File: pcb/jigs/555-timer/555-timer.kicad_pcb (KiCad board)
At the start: 2 copper layers, 16.5 x 15.5 mm, 17 parts, among them J1 Pin headers, J2 Pin headers, U1 NE555

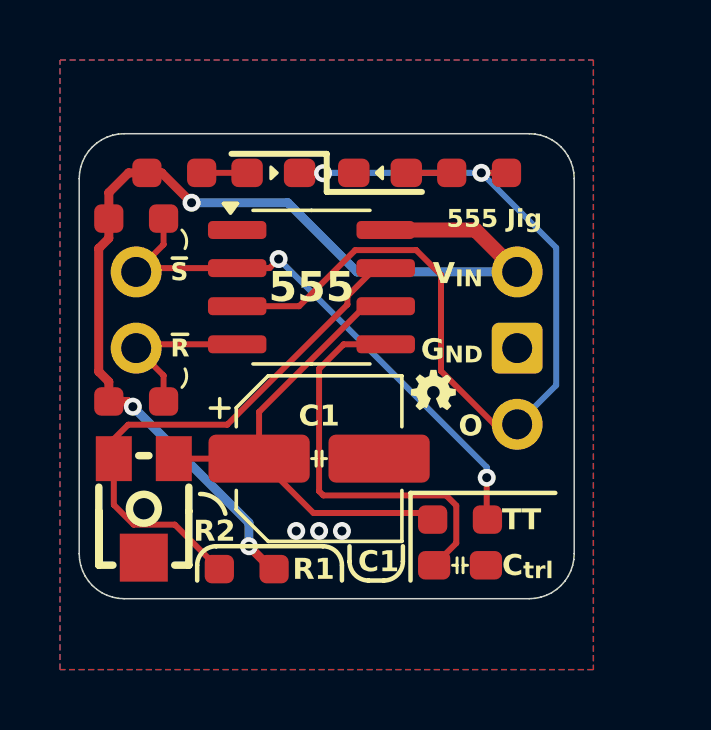
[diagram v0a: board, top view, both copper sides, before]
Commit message: Fix indicator LED order on 555-timer jig
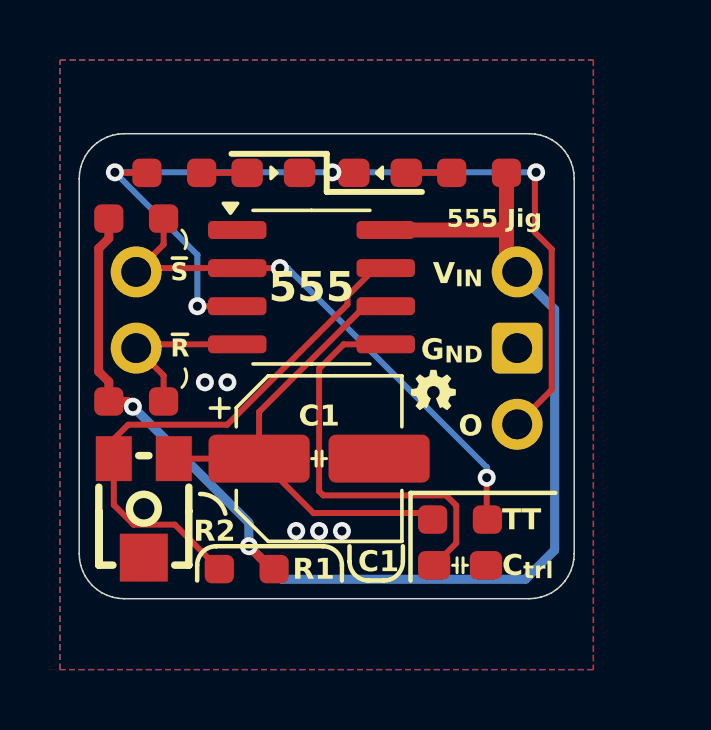
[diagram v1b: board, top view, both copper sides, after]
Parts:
- moved R5 10.2 mm to (135.9, 80.5), turned to 180 degrees
- moved R6 10.2 mm to (125.7, 80.5), turned to 0 degrees
- moved LED1 3.56 mm to (132.6, 80.5), turned to 0 degrees
- moved LED2 3.56 mm to (129.0, 80.5), turned to 180 degrees
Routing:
- net +5V: track 35.7 -> 43.0 mm, vias 3 -> 2
- net Output: track 31.2 -> 31.9 mm, vias 2 -> 4
- net GND: vias 3 -> 5

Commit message: Fix potentiometer pinout on 555-timer jig
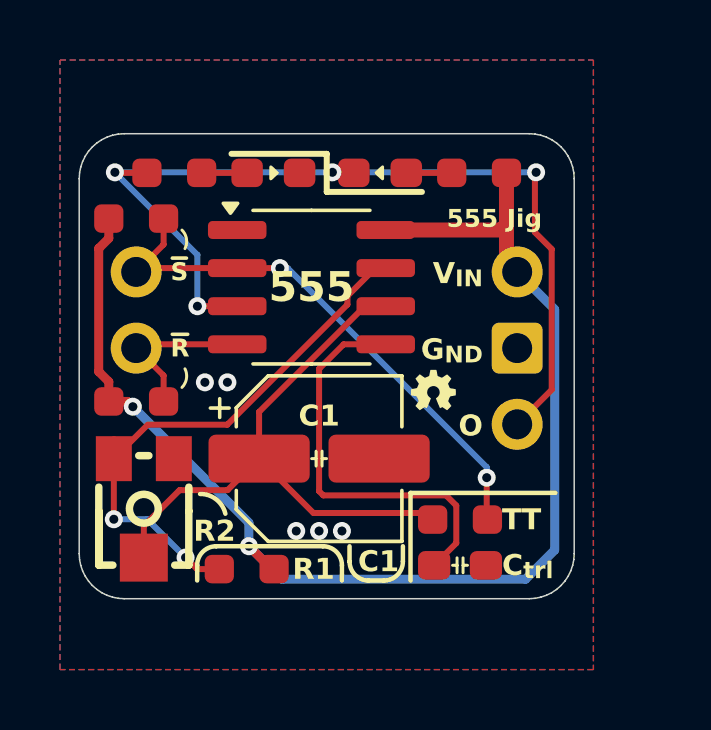
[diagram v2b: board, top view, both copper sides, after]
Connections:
- RV1 pad 1: Net-(U1-Threshold) -> unconnected-(RV1-Pad1)
- RV1 pad 2: unconnected-(RV1-Pad2) -> Net-(U1-Threshold)
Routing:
- net Net-(U1-Threshold): track 16.7 -> 19.7 mm
- net Net-(U1-Discharge): track 18.2 -> 18.7 mm, vias 0 -> 2
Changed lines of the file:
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@@
 	(net 9 "Net-(LED1-A)")
 	(net 10 "Net-(LED2-A)")
-	(net 11 "unconnected-(RV1-Pad2)")
+	(net 11 "unconnected-(RV1-Pad1)")
 	(footprint "custom:C_0603_1608Metric_Pad1.08x0.95mm_HandSolder"
 		(layer "F.Cu")
@@
 			(size 1.2 1.5)
 			(layers "F.Cu" "F.Paste" "F.Mask")
-			(net 3 "Net-(U1-Threshold)")
+			(net 11 "unconnected-(RV1-Pad1)")
 			(pinfunction "1")
-			(pintype "passive")
+			(pintype "passive+no_connect")
 		)
 		(pad "2" smd rect
@@
 			(size 1.6 1.6)
 			(layers "F.Cu" "F.Paste" "F.Mask")
-			(net 11 "unconnected-(RV1-Pad2)")
+			(net 3 "Net-(U1-Threshold)")
 			(pinfunction "2")
-			(pintype "passive+no_connect")
+			(pintype "passive")
 		)
 		(pad "3" smd rect
@@
 	)
 	(segment
-		(start 128.555 90.044)
-		(end 128.556 90.043)
-		(width 0.2)
-		(layer "F.Cu")
-		(net 3)
-	)
-	(segment
 		(start 128.556 90.043)
 		(end 128.556 88.487)
@@
 	)
 	(segment
-		(start 125.714 90.044)
-		(end 128.555 90.044)
+		(start 132.08 84.963)
+		(end 132.777 84.963)
 		(width 0.2)
 		(layer "F.Cu")
@@
 	)
 	(segment
-		(start 132.08 84.963)
-		(end 132.777 84.963)
+		(start 127.505 91.094)
+		(end 125.906 91.094)
 		(width 0.2)
 		(layer "F.Cu")
@@
 	)
 	(segment
-		(start 130.369 91.856)
-		(end 134.1235 91.856)
+		(start 128.556 90.043)
+		(end 127.505 91.094)
 		(width 0.2)
 		(layer "F.Cu")
@@
 	)
 	(segment
-		(start 123.714 91.583)
-		(end 124.375 92.244)
+		(start 124.714 92.286)
+		(end 124.714 93.344)
 		(width 0.2)
 		(layer "F.Cu")
-		(net 4)
+		(net 3)
 	)
 	(segment
-		(start 124.375 92.244)
-		(end 125.7485 92.244)
+		(start 125.906 91.094)
+		(end 124.714 92.286)
 		(width 0.2)
 		(layer "F.Cu")
-		(net 4)
+		(net 3)
 	)
 	(segment
-		(start 123.714 89.392)
-		(end 124.193 88.913)
+		(start 130.369 91.856)
+		(end 134.1235 91.856)
+		(width 0.2)
+		(layer "F.Cu")
+		(net 3)
+	)
+	(segment
+		(start 127.495 88.913)
+		(end 124.845 88.913)
 		(width 0.2)
 		(layer "F.Cu")
@@
 	)
 	(segment
+		(start 124.845 88.913)
+		(end 123.714 90.044)
+		(width 0.2)
+		(layer "F.Cu")
+		(net 4)
+	)
+	(segment
 		(start 127.495 88.913)
 		(end 131.502 84.906)
@@
 	)
 	(segment
+		(start 123.714 92.063763)
+		(end 123.714 90.044)
+		(width 0.2)
+		(layer "F.Cu")
+		(net 4)
+	)
+	(segment
 		(start 131.502 84.906)
 		(end 131.502 84.622448)
@@
 	)
 	(segment
-		(start 125.7485 92.244)
-		(end 127.2305 93.726)
+		(start 127.2305 93.726)
+		(end 126.490002 93.726)
 		(width 0.2)
 		(layer "F.Cu")
@@
 	)
 	(segment
-		(start 124.193 88.913)
-		(end 127.495 88.913)
+		(start 126.490002 93.726)
+		(end 126.105766 93.341764)
 		(width 0.2)
 		(layer "F.Cu")
 		(net 4)
 	)
+	(via
+		(at 126.105766 93.341764)
+		(size 0.6)
+		(drill 0.3)
+		(layers "F.Cu" "B.Cu")
+		(net 4)
+	)
+	(via
+		(at 123.714 92.063763)
+		(size 0.6)
+		(drill 0.3)
+		(layers "F.Cu" "B.Cu")
+		(net 4)
+	)
 	(segment
-		(start 123.714 90.044)
-		(end 123.714 91.583)
+		(start 124.827765 92.063763)
+		(end 126.105766 93.341764)
 		(width 0.2)
-		(layer "F.Cu")
+		(layer "B.Cu")
+		(net 4)
+	)
+	(segment
+		(start 123.714 92.063763)
+		(end 124.827765 92.063763)
+		(width 0.2)
+		(layer "B.Cu")
 		(net 4)
 	)

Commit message: Update 555-timer jig silkscreen info
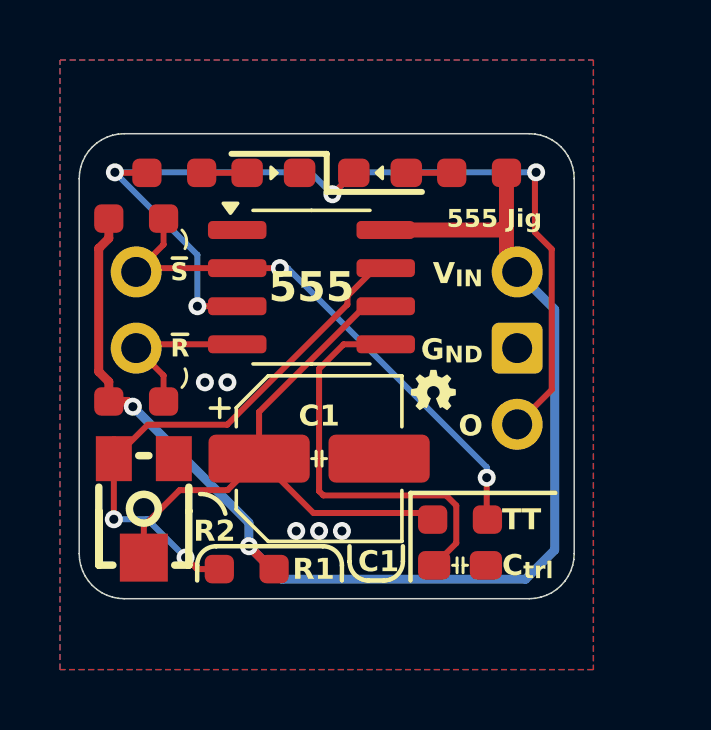
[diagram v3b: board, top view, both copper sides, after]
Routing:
- net Output: track 31.9 -> 32.8 mm
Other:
- board text added: "pcb.smkent.net"
- board text added: "rev 2"
- board text removed: "github.com/smkent/pcb"

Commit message: Change 555-timer jig front title string and font
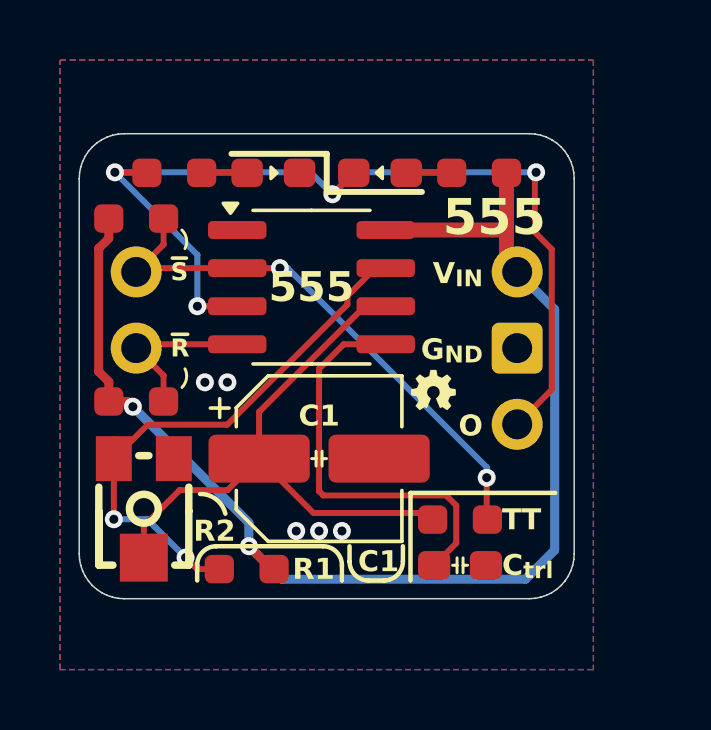
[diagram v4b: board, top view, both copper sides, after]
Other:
- board text removed: "555 Jig"
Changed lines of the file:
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@@
 		)
 	)
-	(gr_text "555 Jig"
-		(at 136.398 82.042 0)
+	(gr_text "555"
+		(at 136.398 82 0)
 		(layer "F.SilkS")
 		(effects
 			(font
-				(size 0.6 0.6)
+				(face "Bitter Black")
+				(size 1.2 1.2)
 				(thickness 0.2)
 				(bold yes)
 			)
 		)
+		(render_cache "555" 0
+			(polygon
+				(pts
+					(xy 135.431384 82.519981) (xy 135.367919 82.517641) (xy 135.303552 82.510622) (xy 135.238283 82.498923)
+					(xy 135.172113 82.482544) (xy 135.105041 82.461485) (xy 135.037068 82.435746) (xy 135.009626 82.42414)
+					(xy 135.098726 82.188788) (xy 135.157307 82.21143) (xy 135.215889 82.230298) (xy 135.242927 82.237734)
+					(xy 135.303971 82.250357) (xy 135.364271 82.256037) (xy 135.375697 82.256199) (xy 135.435316 82.249827)
+					(xy 135.458935 82.242717) (xy 135.508502 82.209324) (xy 135.515209 82.200805) (xy 135.534464 82.144655)
+					(xy 135.535432 82.124894) (xy 135.5251 82.066349) (xy 135.494106 82.028467) (xy 135.437558 82.004098)
+					(xy 135.379214 81.994762) (xy 135.320481 81.991189) (xy 135.260777 81.989363) (xy 135.207756 81.9889)
+					(xy 135.080261 81.9889) (xy 135.103708 81.305117) (xy 135.841126 81.305117) (xy 135.836144 81.565676)
+					(xy 135.345509 81.565676) (xy 135.441349 81.508523) (xy 135.424643 81.814217) (xy 135.337302 81.743582)
+					(xy 135.439591 81.743582) (xy 135.501374 81.745179) (xy 135.567098 81.75108) (xy 135.625979 81.761328)
+					(xy 135.68489 81.778364) (xy 135.710994 81.789011) (xy 135.762691 81.817347) (xy 135.809529 81.855358)
+					(xy 135.848157 81.905103) (xy 135.853729 81.915041) (xy 135.878092 81.973639) (xy 135.891464 82.032441)
+					(xy 135.896479 82.096509) (xy 135.89652 82.103205) (xy 135.893589 82.163254) (xy 135.883061 82.226008)
+					(xy 135.864875 82.282496) (xy 135.835264 82.338558) (xy 135.797284 82.386711) (xy 135.752255 82.427306)
+					(xy 135.700179 82.460343) (xy 135.668202 82.475431) (xy 135.606693 82.496967) (xy 135.54867 82.510193)
+					(xy 135.487496 82.51785)
+				)
+			)
+			(polygon
+				(pts
+					(xy 136.370449 82.519981) (xy 136.306984 82.517641) (xy 136.242617 82.510622) (xy 136.177348 82.498923)
+					(xy 136.111178 82.482544) (xy 136.044106 82.461485) (xy 135.976133 82.435746) (xy 135.948691 82.42414)
+					(xy 136.03779 82.188788) (xy 136.096372 82.21143) (xy 136.154954 82.230298) (xy 136.181991 82.237734)
+					(xy 136.243036 82.250357) (xy 136.303336 82.256037) (xy 136.314762 82.256199) (xy 136.374381 82.249827)
+					(xy 136.398 82.242717) (xy 136.447567 82.209324) (xy 136.454273 82.200805) (xy 136.473529 82.144655)
+					(xy 136.474497 82.124894) (xy 136.464165 82.066349) (xy 136.433171 82.028467) (xy 136.376622 82.004098)
+					(xy 136.318279 81.994762) (xy 136.259546 81.991189) (xy 136.199842 81.989363) (xy 136.146821 81.9889)
+					(xy 136.019326 81.9889) (xy 136.042773 81.305117) (xy 136.780191 81.305117) (xy 136.775209 81.565676)
+					(xy 136.284573 81.565676) (xy 136.380414 81.508523) (xy 136.363708 81.814217) (xy 136.276367 81.743582)
+					(xy 136.378656 81.743582) (xy 136.440439 81.745179) (xy 136.506163 81.75108) (xy 136.565044 81.761328)
+					(xy 136.623955 81.778364) (xy 136.650058 81.789011) (xy 136.701756 81.817347) (xy 136.748594 81.855358)
+					(xy 136.787222 81.905103) (xy 136.792794 81.915041) (xy 136.817157 81.973639) (xy 136.830529 82.032441)
+					(xy 136.835544 82.096509) (xy 136.835585 82.103205) (xy 136.832654 82.163254) (xy 136.822126 82.226008)
+					(xy 136.80394 82.282496) (xy 136.774329 82.338558) (xy 136.736349 82.386711) (xy 136.69132 82.427306)
+					(xy 136.639244 82.460343) (xy 136.607267 82.475431) (xy 136.545757 82.496967) (xy 136.487734 82.510193)
+					(xy 136.426561 82.51785)
+				)
+			)
+			(polygon
+				(pts
+					(xy 137.309514 82.519981) (xy 137.246049 82.517641) (xy 137.181682 82.510622) (xy 137.116413 82.498923)
+					(xy 137.050243 82.482544) (xy 136.983171 82.461485) (xy 136.915197 82.435746) (xy 136.887756 82.42414)
+					(xy 136.976855 82.188788) (xy 137.035437 82.21143) (xy 137.094019 82.230298) (xy 137.121056 82.237734)
+					(xy 137.182101 82.250357) (xy 137.242401 82.256037) (xy 137.253827 82.256199) (xy 137.313446 82.249827)
+					(xy 137.337065 82.242717) (xy 137.386632 82.209324) (xy 137.393338 82.200805) (xy 137.412594 82.144655)
+					(xy 137.413562 82.124894) (xy 137.40323 82.066349) (xy 137.372236 82.028467) (xy 137.315687 82.004098)
+					(xy 137.257344 81.994762) (xy 137.198611 81.991189) (xy 137.138907 81.989363) (xy 137.085885 81.9889)
+					(xy 136.958391 81.9889) (xy 136.981838 81.305117) (xy 137.719256 81.305117) (xy 137.714273 81.565676)
+					(xy 137.223638 81.565676) (xy 137.319479 81.508523) (xy 137.302773 81.814217) (xy 137.215432 81.743582)
+					(xy 137.317721 81.743582) (xy 137.379503 81.745179) (xy 137.445228 81.75108) (xy 137.504109 81.761328)
+					(xy 137.56302 81.778364) (xy 137.589123 81.789011) (xy 137.640821 81.817347) (xy 137.687658 81.855358)
+					(xy 137.726287 81.905103) (xy 137.731859 81.915041) (xy 137.756222 81.973639) (xy 137.769594 82.032441)
+					(xy 137.774608 82.096509) (xy 137.77465 82.103205) (xy 137.771719 82.163254) (xy 137.761191 82.226008)
+					(xy 137.743005 82.282496) (xy 137.713394 82.338558) (xy 137.675414 82.386711) (xy 137.630385 82.427306)
+					(xy 137.578309 82.460343) (xy 137.546332 82.475431) (xy 137.484822 82.496967) (xy 137.426799 82.510193)
+					(xy 137.365626 82.51785)
+				)
+			)
+		)

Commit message: Update PCB projects for footprint updates
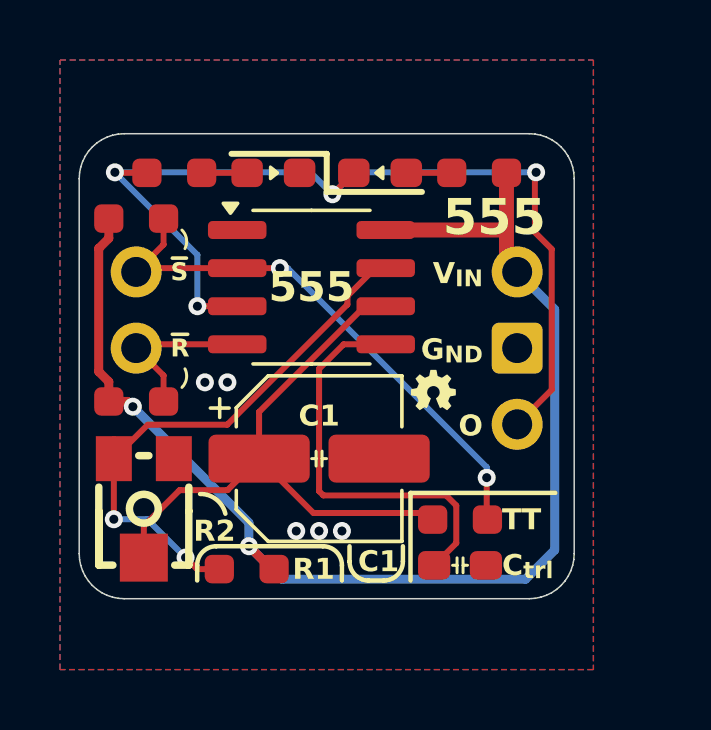
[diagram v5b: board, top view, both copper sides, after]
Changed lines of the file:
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@@
 		(fp_poly
 			(pts
-				(xy 0.085166 -0.2) (xy 0.085166 0.2) (xy -0.130834 0)
+				(xy 0.1 -0.2) (xy 0.1 0.2) (xy -0.15 0)
 			)
 			(stroke
@@
 		(fp_poly
 			(pts
-				(xy 0.085166 -0.2) (xy 0.085166 0.2) (xy -0.130834 0)
-			)
-			(stroke
+				(xy 0.1 -0.2) (xy 0.1 0.2) (xy -0.15 0)
+			)
+			(stroke
